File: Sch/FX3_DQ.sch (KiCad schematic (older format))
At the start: 14 parts, among them IC1 CYUSB3014

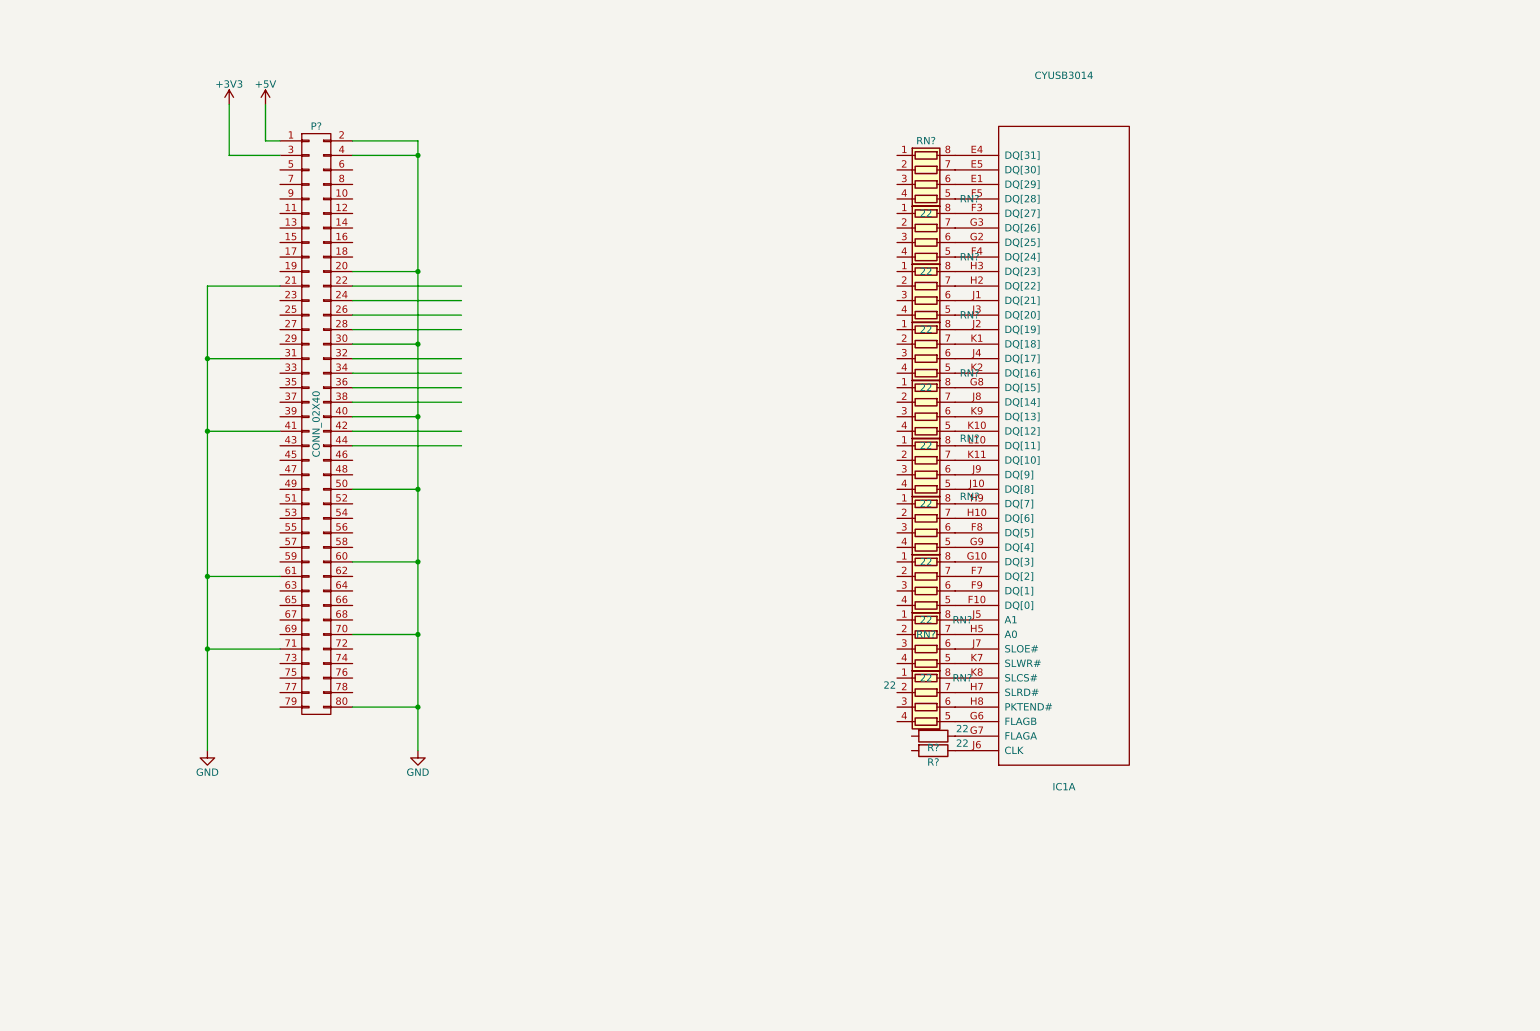
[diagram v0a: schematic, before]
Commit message: Add ADC, CN1/CN2
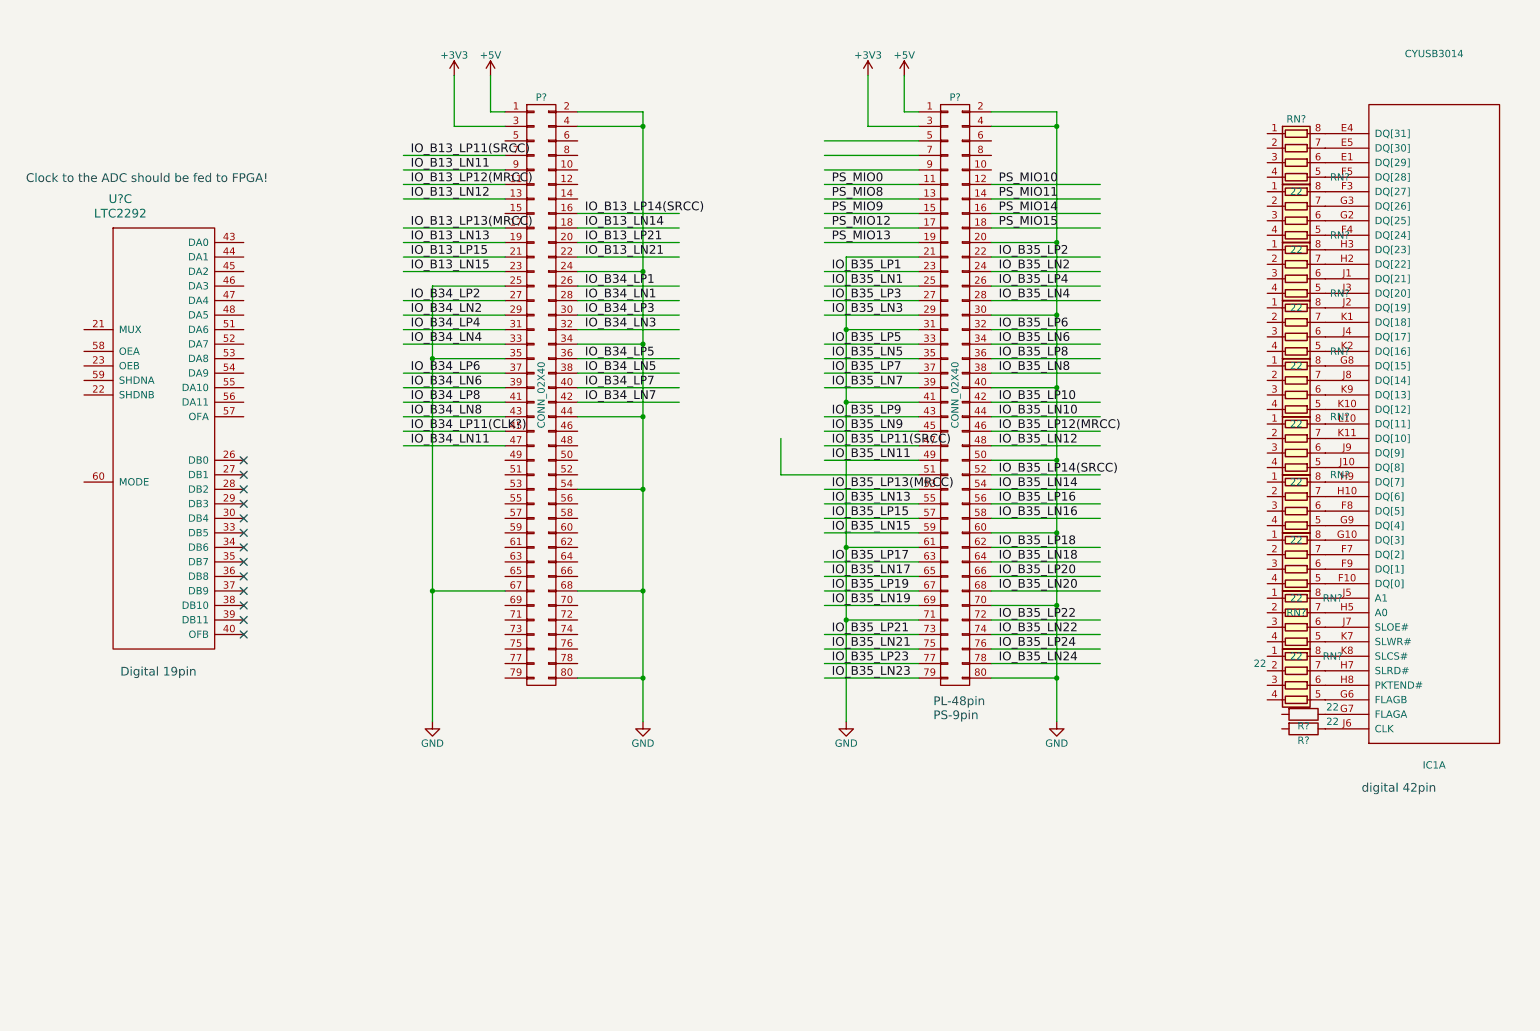
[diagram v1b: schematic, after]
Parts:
- added P?: CONN_02X40, symbol CONN_02X40
- added U?: LTC2292, symbol LTC2292
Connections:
- net labels added: IO_B13_LN11, IO_B13_LN12, IO_B13_LN13, IO_B13_LN14, IO_B13_LN15, IO_B13_LN21, IO_B13_LP11(SRCC), IO_B13_LP12(MRCC), IO_B13_LP13(MRCC), IO_B13_LP14(SRCC), IO_B13_LP15, IO_B13_LP21, IO_B34_LN1, IO_B34_LN11, IO_B34_LN2, IO_B34_LN3, IO_B34_LN4, IO_B34_LN5, IO_B34_LN6, IO_B34_LN7, IO_B34_LN8, IO_B34_LP1, IO_B34_LP11(CLK?), IO_B34_LP2, IO_B34_LP3, IO_B34_LP4, IO_B34_LP5, IO_B34_LP6, IO_B34_LP7, IO_B34_LP8, IO_B35_LN1, IO_B35_LN10, IO_B35_LN11, IO_B35_LN12, IO_B35_LN13, IO_B35_LN14, IO_B35_LN15, IO_B35_LN16, IO_B35_LN17, IO_B35_LN18, IO_B35_LN19, IO_B35_LN2, IO_B35_LN20, IO_B35_LN21, IO_B35_LN22, IO_B35_LN23, IO_B35_LN24, IO_B35_LN3, IO_B35_LN4, IO_B35_LN5, IO_B35_LN6, IO_B35_LN7, IO_B35_LN8, IO_B35_LN9, IO_B35_LP1, IO_B35_LP10, IO_B35_LP11(SRCC), IO_B35_LP12(MRCC), IO_B35_LP13(MRCC), IO_B35_LP14(SRCC), IO_B35_LP15, IO_B35_LP16, IO_B35_LP17, IO_B35_LP18, IO_B35_LP19, IO_B35_LP2, IO_B35_LP20, IO_B35_LP21, IO_B35_LP22, IO_B35_LP23, IO_B35_LP24, IO_B35_LP3, IO_B35_LP4, IO_B35_LP5, IO_B35_LP6, IO_B35_LP7, IO_B35_LP8, IO_B35_LP9, PS_MIO0, PS_MIO10, PS_MIO11, PS_MIO12, PS_MIO13, PS_MIO14, PS_MIO15, PS_MIO8, PS_MIO9
- wire segments 30 -> 129
- no-connect marks 0 -> 13
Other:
- note added: "Clock to the ADC should be fed to FPGA!"
- note added: "Digital 19pin"
- note added: "PL-48pin\nPS-9pin"
- note added: "digital 42pin"
- moved on the sheet: IC1A, P?, R?, RN?

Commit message: modify
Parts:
- gave numbers to parts that had none: 15
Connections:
- net labels added: FX3_CTL[15], FX3_GPIO[45], FX3_RESET#
- wire segments 129 -> 188
- no-connect marks 13 -> 16
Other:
- note added: "Bank13,34,35=3.3V"
- moved on the sheet: IC1A, R11, R12, RN10, RN11, RN2, RN3, RN4, RN5, RN6, RN7, RN8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

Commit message: update
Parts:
- added C53: 0.1u, symbol C
- added J1: JP4, symbol JP4
- added R24, R25, R26: 1k, symbol R
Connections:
- net labels added: FX3_GPIO[26], FX3_GPIO[27]
- wire segments 188 -> 213
- no-connect marks 16 -> 53

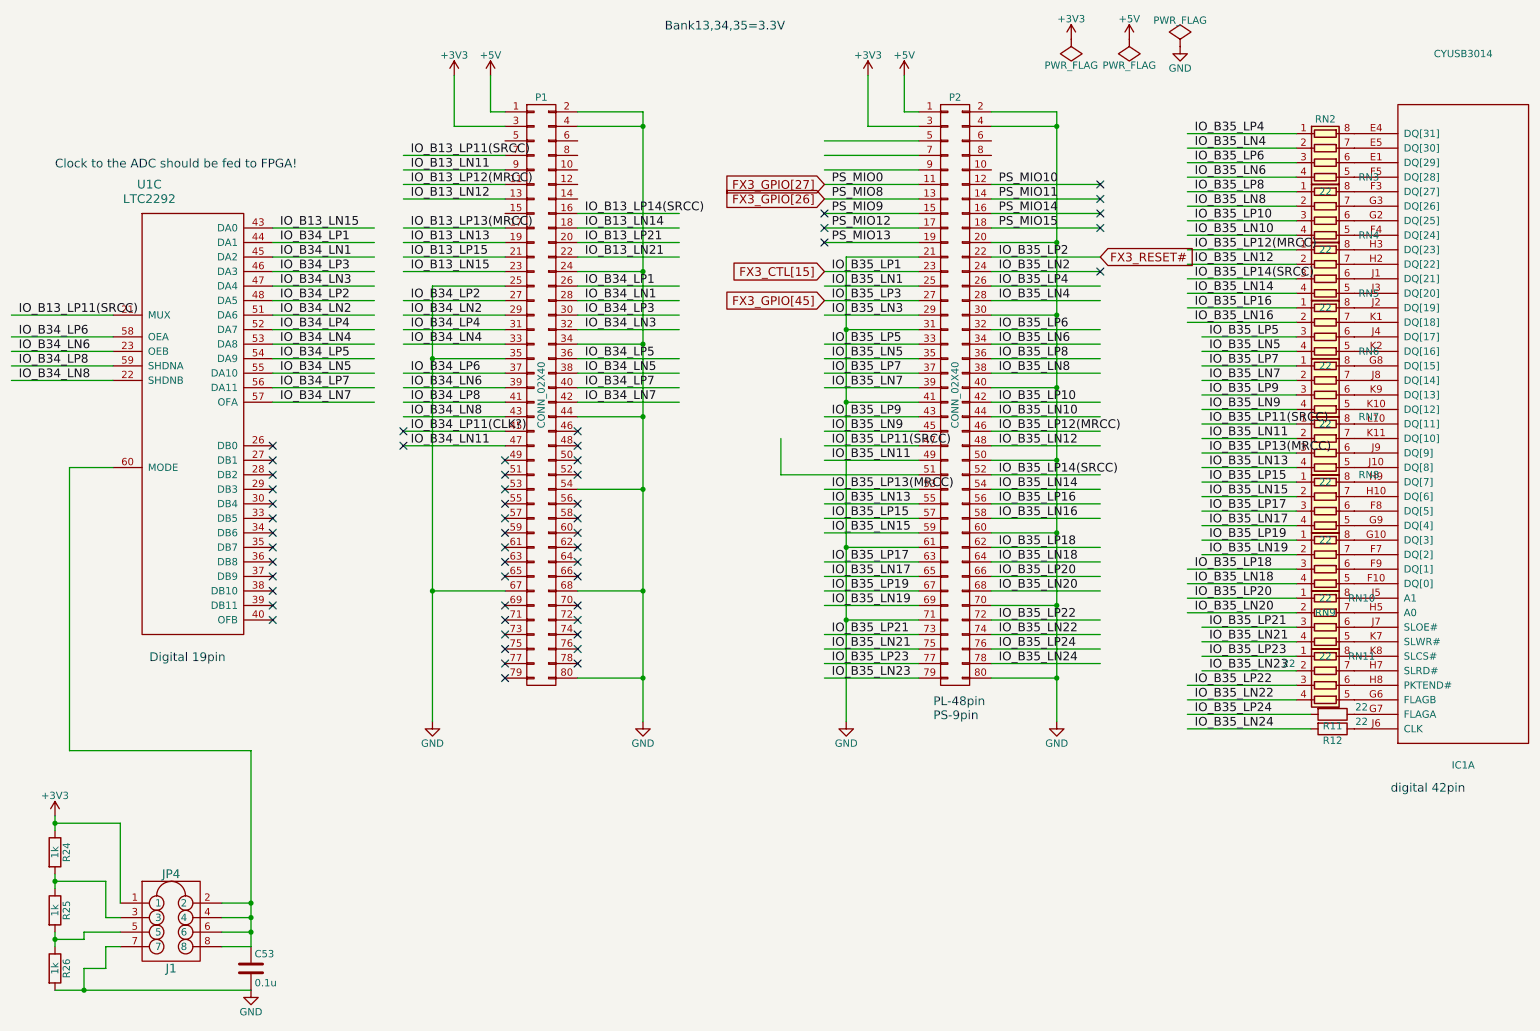
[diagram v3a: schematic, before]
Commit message: Add 1.2V
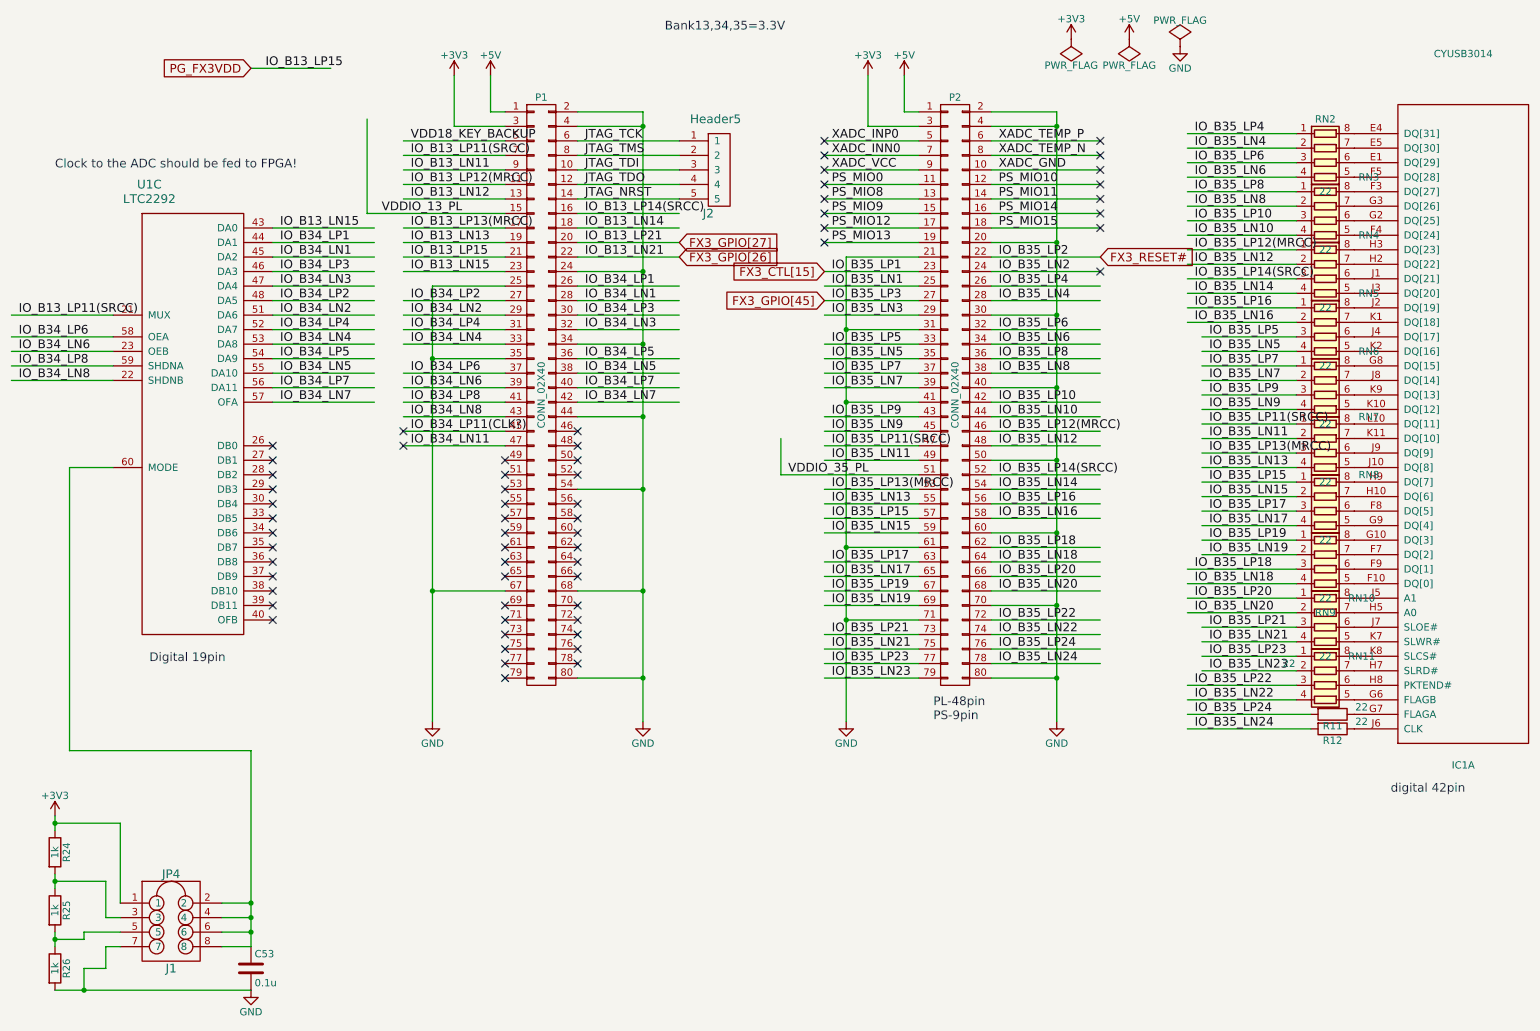
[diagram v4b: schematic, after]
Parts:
- added J2: Header5, symbol Header5
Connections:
- net labels added: JTAG_NRST, JTAG_TCK, JTAG_TDI, JTAG_TDO, JTAG_TMS, PG_FX3VDD, VDD18_KEY_BACKUP, VDDIO_13_PL, VDDIO_35_PL, XADC_GND, XADC_INN0, XADC_INP0, XADC_TEMP_N, XADC_TEMP_P, XADC_VCC
- wire segments 213 -> 225
- no-connect marks 53 -> 61
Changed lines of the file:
@@
 $Descr A4 11693 8268
 encoding utf-8
-Sheet 4 6
+Sheet 4 7
 Title ""
 Date ""
@@
 	-1   0    0    1
 $EndComp
-NoConn ~ 6200 2050
 NoConn ~ 6200 2150
 NoConn ~ 6200 2250
@@
 Text Label 650  2750 0    60   ~ 0
 IO_B13_LP11(SRCC)
-Text GLabel 6200 1850 0    60   Input ~ 0
+Text GLabel 5200 2250 2    60   Input ~ 0
 FX3_GPIO[27]
-Text GLabel 6200 1950 0    60   Input ~ 0
+Text GLabel 5200 2350 2    60   Input ~ 0
 FX3_GPIO[26]
 $Comp
@@
 	2250 7100 2050 7100
 Wire Wire Line
-	2050 7000 2250 7000
+	2250 7000 2050 7000
 Wire Wire Line
 	2250 5750 2250 7100
@@
 	1000 5750 2250 5750
 Connection ~ 2250 6800
+Text GLabel 2250 1050 0    60   Input ~ 0
+PG_FX3VDD
+Wire Wire Line
+	2250 1050 2800 1050
+Text Label 2350 1050 0    60   ~ 0
+IO_B13_LP15
+NoConn ~ 6200 2050
+NoConn ~ 6200 1950
+NoConn ~ 6200 1850
+Text Label 6250 1550 0    60   ~ 0
+XADC_INP0
+Text Label 6250 1650 0    60   ~ 0
+XADC_INN0
+NoConn ~ 6200 1550
+NoConn ~ 6200 1650
+Text Label 6250 1750 0    60   ~ 0
+XADC_VCC
+NoConn ~ 6200 1750
+Wire Wire Line
+	7350 1550 8100 1550
+Wire Wire Line
+	7350 1650 8100 1650
+Wire Wire Line
+	7350 1750 8100 1750
+NoConn ~ 8100 1550
+NoConn ~ 8100 1650
+NoConn ~ 8100 1750
+Text Label 7400 1550 0    60   ~ 0
+XADC_TEMP_P
+Text Label 7400 1650 0    60   ~ 0
+XADC_TEMP_N
+Text Label 7400 1750 0    60   ~ 0
+XADC_GND
+Text Label 5950 3850 0    60   ~ 0
+VDDIO_35_PL
+Wire Wire Line
+	4000 2050 3050 2050
+Wire Wire Line
+	3050 2050 3050 1400
+Text Label 3150 2050 0    60   ~ 0
+VDDIO_13_PL
+Wire Wire Line
+	4000 1550 3300 1550
+Text Label 3350 1550 0    60   ~ 0
+VDD18_KEY_BACKUP
+Wire Wire Line
+	4500 1550 5200 1550
+Wire Wire Line
+	4500 1650 5200 1650
+Wire Wire Line
+	4500 1750 5200 1750
+Wire Wire Line
+	4500 1950 5200 1950
+Text Label 4550 1550 0    60   ~ 0
+JTAG_TCK
+Text Label 4550 1650 0    60   ~ 0
+JTAG_TMS
+Text Label 4550 1750 0    60   ~ 0
+JTAG_TDI
+Text Label 4550 1850 0    60   ~ 0
+JTAG_TDO
+Text Label 4550 1950 0    60   ~ 0
+JTAG_NRST
+Wire Wire Line
+	4500 1850 5200 1850
+$Comp
+L Header5 J2
+U 1 1 58A52616
+P 5400 1750
+F 0 "J2" H 5400 1450 60  0000 C CNN
+F 1 "Header5" H 5450 2100 60  0000 C CNN
+F 2 "" H 5400 1850 60  0001 C CNN
+F 3 "" H 5400 1850 60  0001 C CNN
+	1    5400 1750
+	1    0    0    -1
+$EndComp
 $EndSCHEMATC

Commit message: modify
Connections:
- no-connect marks 61 -> 65
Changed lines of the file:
@@
 Text Label 650  2900 0    60   ~ 0
 IO_B34_LP6
-NoConn ~ 8100 2450
 NoConn ~ 3300 3550
 NoConn ~ 3300 3650
@@
 Text Label 650  2750 0    60   ~ 0
 IO_B13_LP11(SRCC)
-Text GLabel 5200 2250 2    60   Input ~ 0
+Text GLabel 8100 2450 2    60   Input ~ 0
 FX3_GPIO[27]
-Text GLabel 5200 2350 2    60   Input ~ 0
+Text GLabel 6200 2750 0    60   Input ~ 0
 FX3_GPIO[26]
 $Comp
@@
 	1    0    0    -1
 $EndComp
+NoConn ~ 5200 2050
+NoConn ~ 5200 2150
+NoConn ~ 5200 2250
+NoConn ~ 5200 2350
+NoConn ~ 6200 2550
 $EndSCHEMATC
